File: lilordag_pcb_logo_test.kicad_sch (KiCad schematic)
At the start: 31 parts, among them J1 USB4105-GF-A, Q5 BC846, Q6 BC846, Q7 SSM3J56MFV, Q8 SSM3J56MFV, SW1 PCM12SMTR

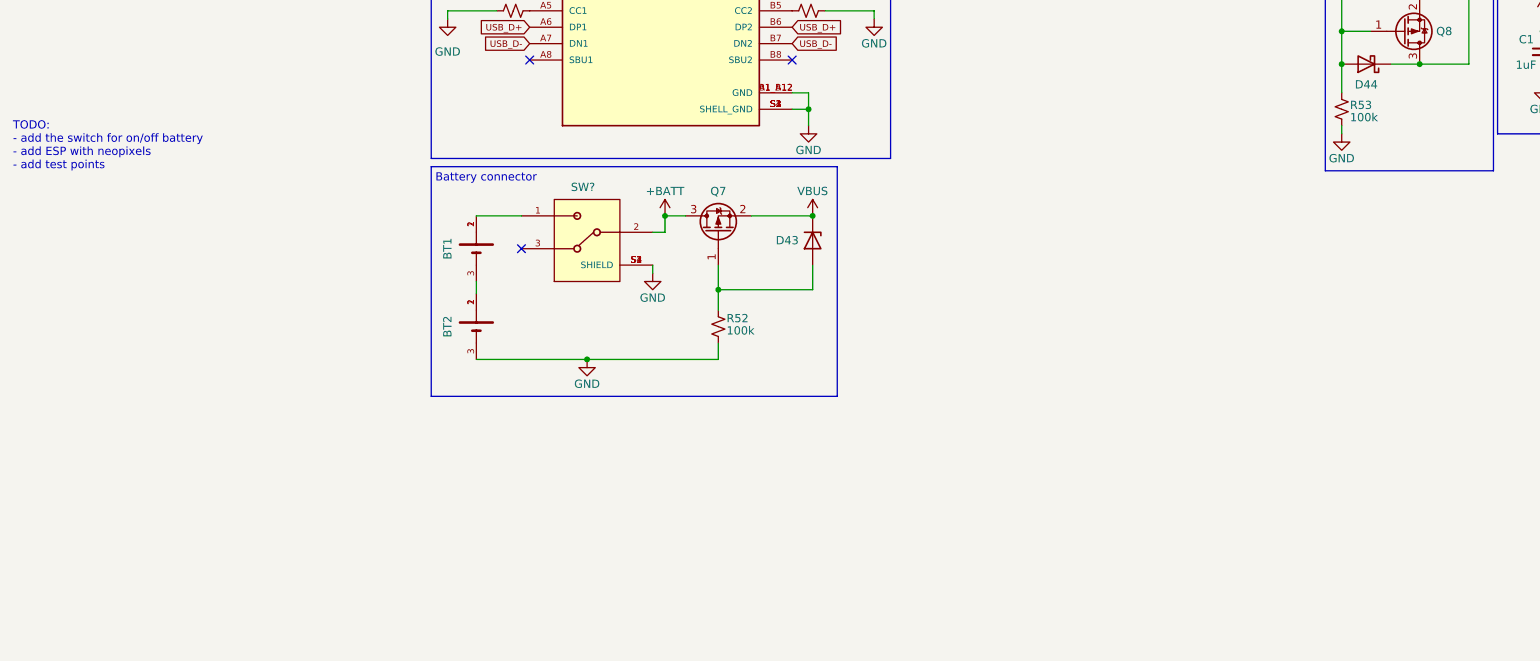
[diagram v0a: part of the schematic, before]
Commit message: Added datasheet for the LED and assigned 3d parts.
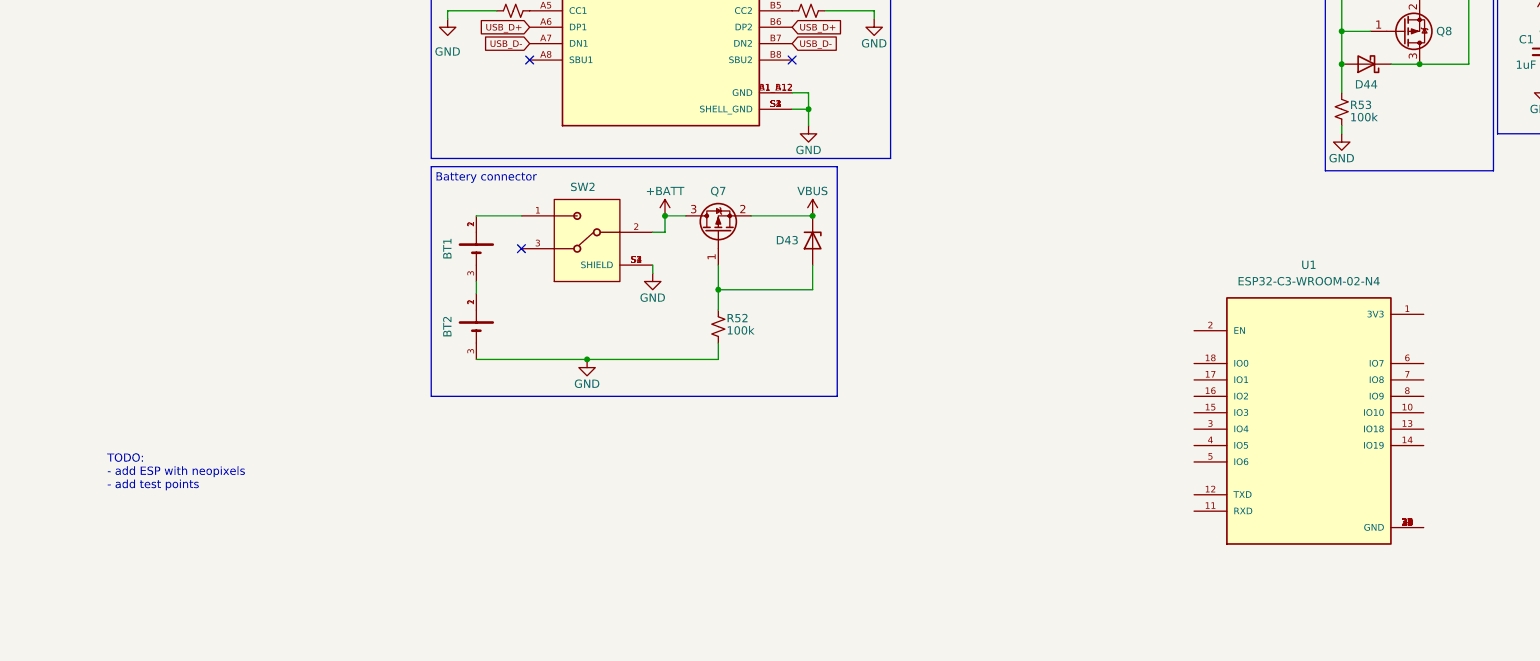
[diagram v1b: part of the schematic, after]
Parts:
- added U1: ESP32-C3-WROOM-02-N4, MODULE_ESP32-C3-WROOM-02-H4, symbol ESP32-C3-WROOM-02-N4:ESP32-C3-WROOM-02-N4
- gave numbers to parts that had none: 1
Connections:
- new net: U1.19 (GND), U1.20 (GND), U1.21 (GND), U1.22 (GND), U1.23 (GND), U1.24 (GND), U1.25 (GND), U1.26 (GND), U1.27 (GND), U1.28 (GND), U1.29 (GND), U1.30 (GND), U1.31 (GND), U1.32 (GND), U1.33 (GND), U1.34 (GND), U1.35 (GND), U1.36 (GND), U1.37 (GND), U1.38 (GND), U1.39 (GND), U1.9 (GND)
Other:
- note added: "TODO: - add ESP with neopixels - add test points"
- note removed: "TODO: - add the switch for on/off battery - add ESP with neopixels - add test points"

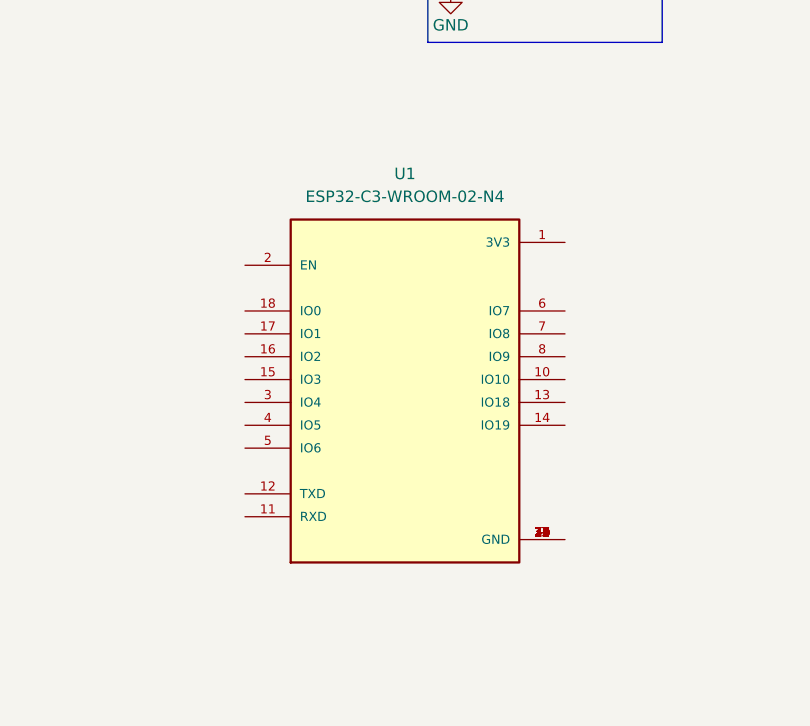
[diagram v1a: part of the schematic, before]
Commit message: Downloaded assets for the esp32-c3-mini.
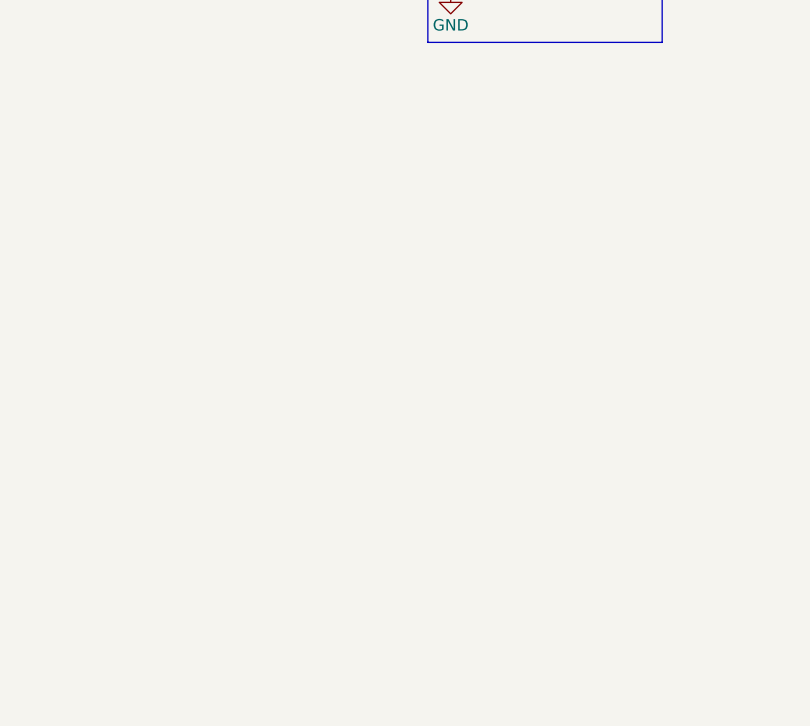
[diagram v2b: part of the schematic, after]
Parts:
- removed U1: ESP32-C3-WROOM-02-N4, MODULE_ESP32-C3-WROOM-02-H4, symbol ESP32-C3-WROOM-02-N4:ESP32-C3-WROOM-02-N4
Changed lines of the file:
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@@
     (pin "1")
-  )
-  (symbol (lib_id "ESP32-C3-WROOM-02-N4:ESP32-C3-WROOM-02-N4") (at 148.59 91.44 0) (unit 1)
-    (in_bom yes) (on_board yes) (fields_autoplaced)
-    (property "Reference" "U1" (id 0) (at 148.59 66.04 0))
-    (property "Value" "ESP32-C3-WROOM-02-N4" (id 1) (at 148.59 68.58 0))
-    (property "Footprint" "MODULE_ESP32-C3-WROOM-02-H4" (id 2) (at 148.59 91.44 0)
-      (effects (font (size 1.27 1.27)) (justify left bottom) hide)
-    )
-    (property "Datasheet" "" (id 3) (at 148.59 91.44 0)
-      (effects (font (size 1.27 1.27)) (justify left bottom) hide)
-    )
-    (property "DESCRIPTION" "WiFi Modules (802.11) (Engineering Samples) SMD module, ESP32-C3, 4MB SPI flash, PCB antenna, -40 C +105 C" (id 4) (at 148.59 91.44 0)
-      (effects (font (size 1.27 1.27)) (justify left bottom) hide)
-    )
-    (property "PRICE" "None" (id 5) (at 148.59 91.44 0)
-      (effects (font (size 1.27 1.27)) (justify left bottom) hide)
-    )
-    (property "MP" "ESP32-C3-WROOM-02-H4" (id 6) (at 148.59 91.44 0)
-      (effects (font (size 1.27 1.27)) (justify left bottom) hide)
-    )
-    (property "AVAILABILITY" "In Stock" (id 7) (at 148.59 91.44 0)
-      (effects (font (size 1.27 1.27)) (justify left bottom) hide)
-    )
-    (property "PURCHASE-URL" "https://pricing.snapeda.com/search/part/ESP32-C3-WROOM-02-H4/?ref=eda" (id 8) (at 148.59 91.44 0)
-      (effects (font (size 1.27 1.27)) (justify left bottom) hide)
-    )
-    (property "MF" "Espressif Systems" (id 9) (at 148.59 91.44 0)
-      (effects (font (size 1.27 1.27)) (justify left bottom) hide)
-    )
-    (property "PACKAGE" "Package" (id 10) (at 148.59 91.44 0)
-      (effects (font (size 1.27 1.27)) (justify left bottom) hide)
-    )
-    (pin "1")
-    (pin "10")
-    (pin "11")
-    (pin "12")
-    (pin "13")
-    (pin "14")
-    (pin "15")
-    (pin "16")
-    (pin "17")
-    (pin "18")
-    (pin "19")
-    (pin "2")
-    (pin "20")
-    (pin "21")
-    (pin "22")
-    (pin "23")
-    (pin "24")
-    (pin "25")
-    (pin "26")
-    (pin "27")
-    (pin "28")
-    (pin "29")
-    (pin "3")
-    (pin "30")
-    (pin "31")
-    (pin "32")
-    (pin "33")
-    (pin "34")
-    (pin "35")
-    (pin "36")
-    (pin "37")
-    (pin "38")
-    (pin "39")
-    (pin "4")
-    (pin "5")
-    (pin "6")
-    (pin "7")
-    (pin "8")
-    (pin "9")
   )
   (symbol (lib_id "power:GND") (at 71.12 44.45 0) (unit 1)
@@
       (reference "SW2") (unit 1) (value "PCM12SMTR") (footprint "PCM12SMTR:SW_PCM12SMTR")
     )
-    (path "/763cf8f4-54d0-4730-ac86-c37b7bfedab3"
-      (reference "U1") (unit 1) (value "ESP32-C3-WROOM-02-N4") (footprint "MODULE_ESP32-C3-WROOM-02-H4")
-    )
     (path "/ff3f1e73-bc2c-4101-bab4-9447a6257bc8"

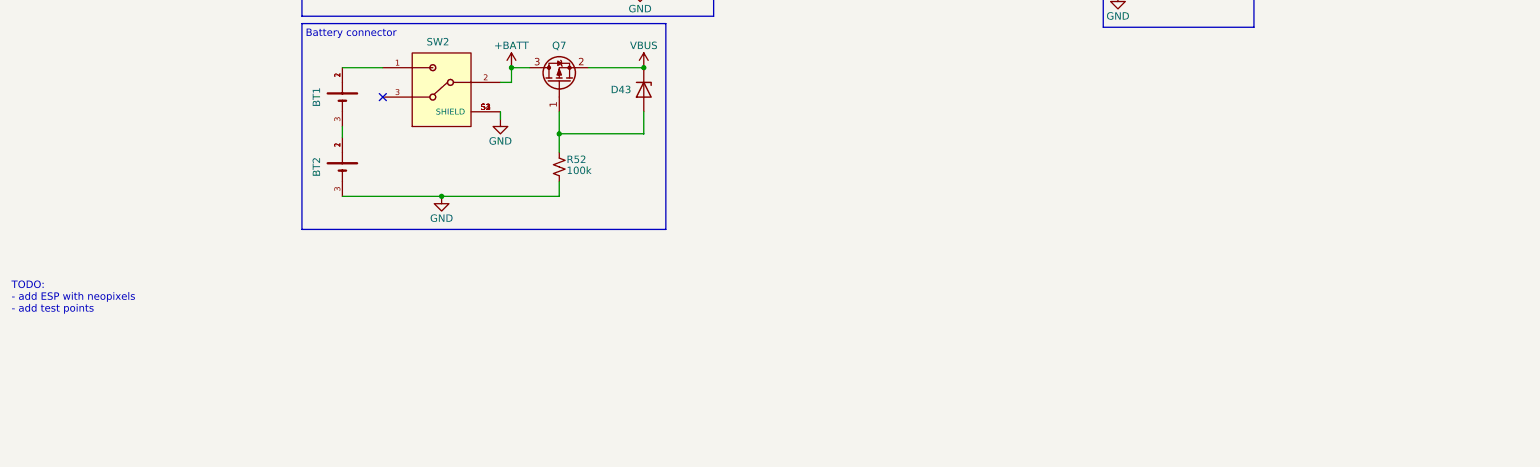
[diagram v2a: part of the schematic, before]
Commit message: Added esp32c3mini to the schematic and the pcb.
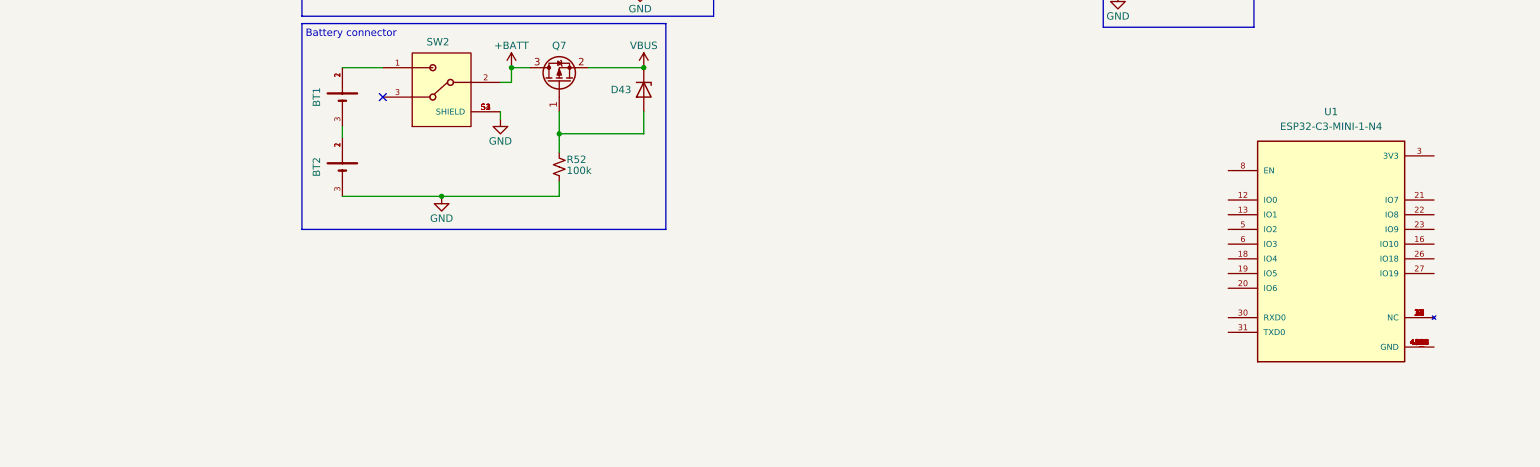
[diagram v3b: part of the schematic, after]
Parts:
- added U1: ESP32-C3-MINI-1-N4, ESP32-C3-MINI:XCVR_ESP32-C3-MINI-1-N4, symbol ESP32-C3-MINI-1-N4:ESP32-C3-MINI-1-N4
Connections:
- new net: U1.1 (GND), U1.11 (GND), U1.14 (GND), U1.2 (GND), U1.36 (GND), U1.37 (GND), U1.38 (GND), U1.39 (GND), U1.40 (GND), U1.41 (GND), U1.42 (GND), U1.43 (GND), U1.44 (GND), U1.45 (GND), U1.46 (GND), U1.47 (GND), U1.48 (GND), U1.49_1 (GND), U1.49_2 (GND), U1.49_3 (GND), U1.49_4 (GND), U1.49_5 (GND), U1.49_6 (GND), U1.49_7 (GND), U1.49_8 (GND), U1.49_9 (GND), U1.50 (GND), U1.51 (GND), U1.52 (GND), U1.53 (GND)
- new net: U1.10 (NC), U1.15 (NC), U1.17 (NC), U1.24 (NC), U1.25 (NC), U1.28 (NC), U1.29 (NC), U1.32 (NC), U1.33 (NC), U1.34 (NC), U1.35 (NC), U1.4 (NC), U1.7 (NC), U1.9 (NC)
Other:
- note removed: "TODO: - add ESP with neopixels - add test points"
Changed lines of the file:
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@@
-    (effects (font (size 1.27 1.27)) (justify left bottom))
-  )
-  (text "TODO:\n- add ESP with neopixels\n- add test points\n" (at -37.465 100.965 0)
     (effects (font (size 1.27 1.27)) (justify left bottom))
   )
@@
     (pin "2")
   )
+  (symbol (lib_id "ESP32-C3-MINI-1-N4:ESP32-C3-MINI-1-N4") (at 190.5 88.9 0) (unit 1)
+    (in_bom yes) (on_board yes) (fields_autoplaced)
+    (property "Reference" "U1" (id 0) (at 190.5 66.04 0))
+    (property "Value" "ESP32-C3-MINI-1-N4" (id 1) (at 190.5 68.58 0))
+    (property "Footprint" "ESP32-C3-MINI:XCVR_ESP32-C3-MINI-1-N4" (id 2) (at 190.5 88.9 0)
+      (effects (font (size 1.27 1.27)) (justify left bottom) hide)
+    )
+    (property "Datasheet" "" (id 3) (at 190.5 88.9 0)
+      (effects (font (size 1.27 1.27)) (justify left bottom) hide)
+    )
+    (property "MAXIMUM_PACKAGE_HEIGHT" "2.55mm" (id 4) (at 190.5 88.9 0)
+      (effects (font (size 1.27 1.27)) (justify left bottom) hide)
+    )
+    (property "MANUFACTURER" "Espressif Systems" (id 5) (at 190.5 88.9 0)
+      (effects (font (size 1.27 1.27)) (justify left bottom) hide)
+    )
+    (property "STANDARD" "Manufacturer Recommendations" (id 6) (at 190.5 88.9 0)
+      (effects (font (size 1.27 1.27)) (justify left bottom) hide)
+    )
+    (property "PARTREV" "v1.0" (id 7) (at 190.5 88.9 0)
+      (effects (font (size 1.27 1.27)) (justify left bottom) hide)
+    )
+    (pin "1")
+    (pin "10")
+    (pin "11")
+    (pin "12")
+    (pin "13")
+    (pin "14")
+    (pin "15")
+    (pin "16")
+    (pin "17")
+    (pin "18")
+    (pin "19")
+    (pin "2")
+    (pin "20")
+    (pin "21")
+    (pin "22")
+    (pin "23")
+    (pin "24")
+    (pin "25")
+    (pin "26")
+    (pin "27")
+    (pin "28")
+    (pin "29")
+    (pin "3")
+    (pin "30")
+    (pin "31")
+    (pin "32")
+    (pin "33")
+    (pin "34")
+    (pin "35")
+    (pin "36")
+    (pin "37")
+    (pin "38")
+    (pin "39")
+    (pin "4")
+    (pin "40")
+    (pin "41")
+    (pin "42")
+    (pin "43")
+    (pin "44")
+    (pin "45")
+    (pin "46")
+    (pin "47")
+    (pin "48")
+    (pin "49_1")
+    (pin "49_2")
+    (pin "49_3")
+    (pin "49_4")
+    (pin "49_5")
+    (pin "49_6")
+    (pin "49_7")
+    (pin "49_8")
+    (pin "49_9")
+    (pin "5")
+    (pin "50")
+    (pin "51")
+    (pin "52")
+    (pin "53")
+    (pin "6")
+    (pin "7")
+    (pin "8")
+    (pin "9")
+  )
   (symbol (lib_id "power:GND") (at 46.99 67.31 0) (unit 1)
     (in_bom yes) (on_board yes)
@@
       (reference "SW2") (unit 1) (value "PCM12SMTR") (footprint "PCM12SMTR:SW_PCM12SMTR")
     )
+    (path "/16ae4e27-6502-4d87-b62e-ae69ab0f8898"
+      (reference "U1") (unit 1) (value "ESP32-C3-MINI-1-N4") (footprint "ESP32-C3-MINI:XCVR_ESP32-C3-MINI-1-N4")
+    )
     (path "/ff3f1e73-bc2c-4101-bab4-9447a6257bc8"

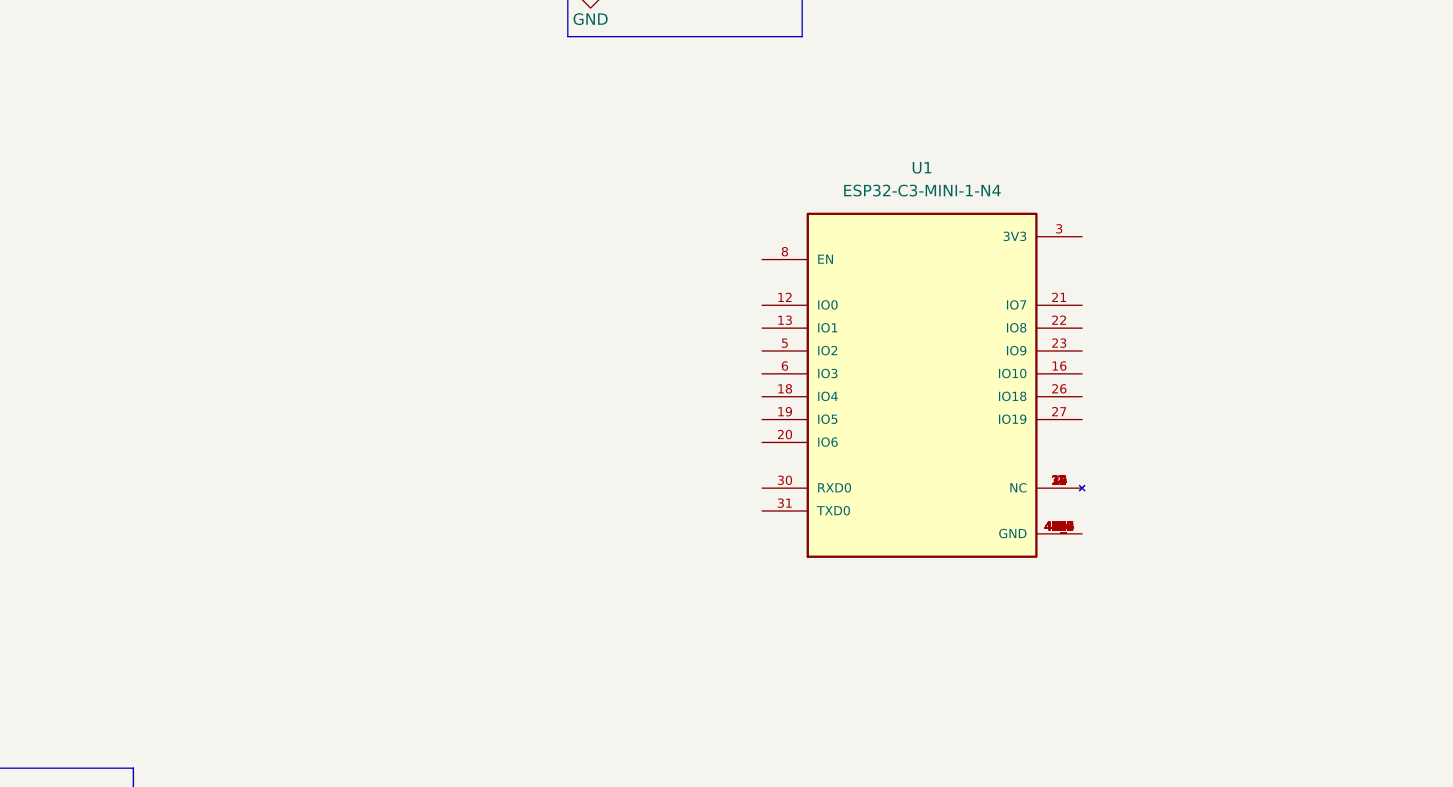
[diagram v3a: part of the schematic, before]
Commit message: Added reset button for the ESP.
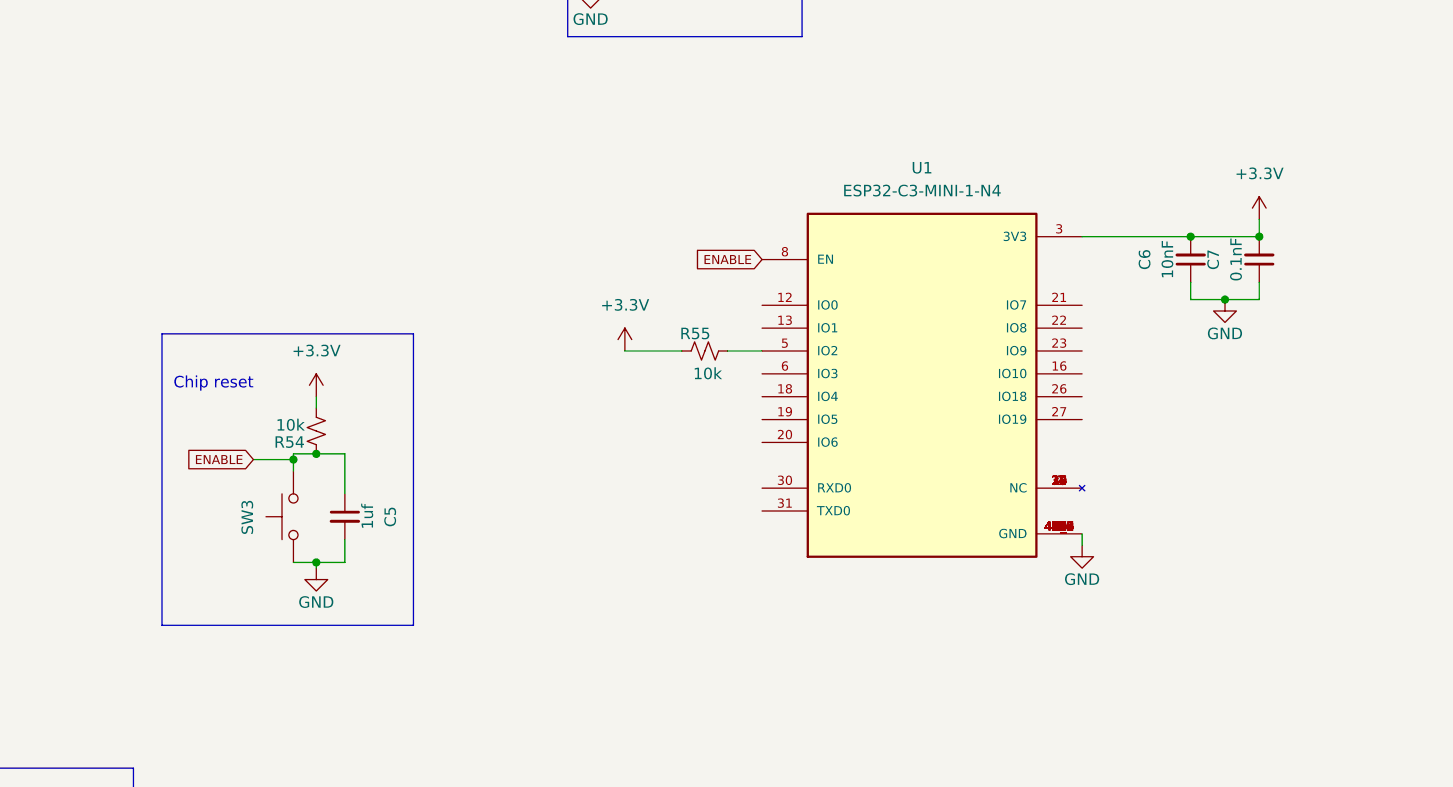
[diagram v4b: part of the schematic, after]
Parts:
- added C5: 1uf, Capacitor_SMD:C_0603_1608Metric_Pad1.08x0.95mm_HandSolder, symbol Device:C_Small
- added C6: 10nF, Capacitor_SMD:C_0603_1608Metric_Pad1.08x0.95mm_HandSolder, symbol Device:C_Small
- added C7: 0.1nF, Capacitor_SMD:C_0603_1608Metric_Pad1.08x0.95mm_HandSolder, symbol Device:C_Small
- added R54, R55: 10k, Resistor_SMD:R_0603_1608Metric_Pad0.98x0.95mm_HandSolder, symbol Device:R_Small_US
- added SW3: SW_MEC_5G, switch-TL3301AF260QG:TL3301AF260QG, symbol Switch:SW_MEC_5G
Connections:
- net +3.3V: now also U1.3 (3V3), C6.2, C7.2, R54.2, R55.1
- net GND: now also U1.1 (GND), U1.11 (GND), U1.14 (GND), U1.2 (GND), U1.36 (GND), U1.37 (GND), U1.38 (GND), U1.39 (GND), U1.40 (GND), U1.41 (GND), U1.42 (GND), U1.43 (GND), U1.44 (GND), U1.45 (GND), U1.46 (GND), U1.47 (GND), U1.48 (GND), U1.49_1 (GND), U1.49_2 (GND), U1.49_3 (GND), U1.49_4 (GND), U1.49_5 (GND), U1.49_6 (GND), U1.49_7 (GND), U1.49_8 (GND), U1.49_9 (GND), U1.50 (GND), U1.51 (GND), U1.52 (GND), U1.53 (GND), C5.2, C6.1, C7.1, SW3.1 (A), SW3.2 (A)
- net at U1.5 (IO2): now also R55.2
- net ENABLE: now reaches U1.8 (EN)
- net ENABLE: now also C5.1, R54.1, SW3.3 (B), SW3.4 (B)
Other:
- note added: "Chip reset"
